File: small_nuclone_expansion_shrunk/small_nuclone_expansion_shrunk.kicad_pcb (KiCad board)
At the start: 2 copper layers, 48.3 x 48.3 mm, 11 parts, among them J1 nuclone_small_left, J2 nuclone_small_right, J3 PINS_1X18, J4 PINS_1X17

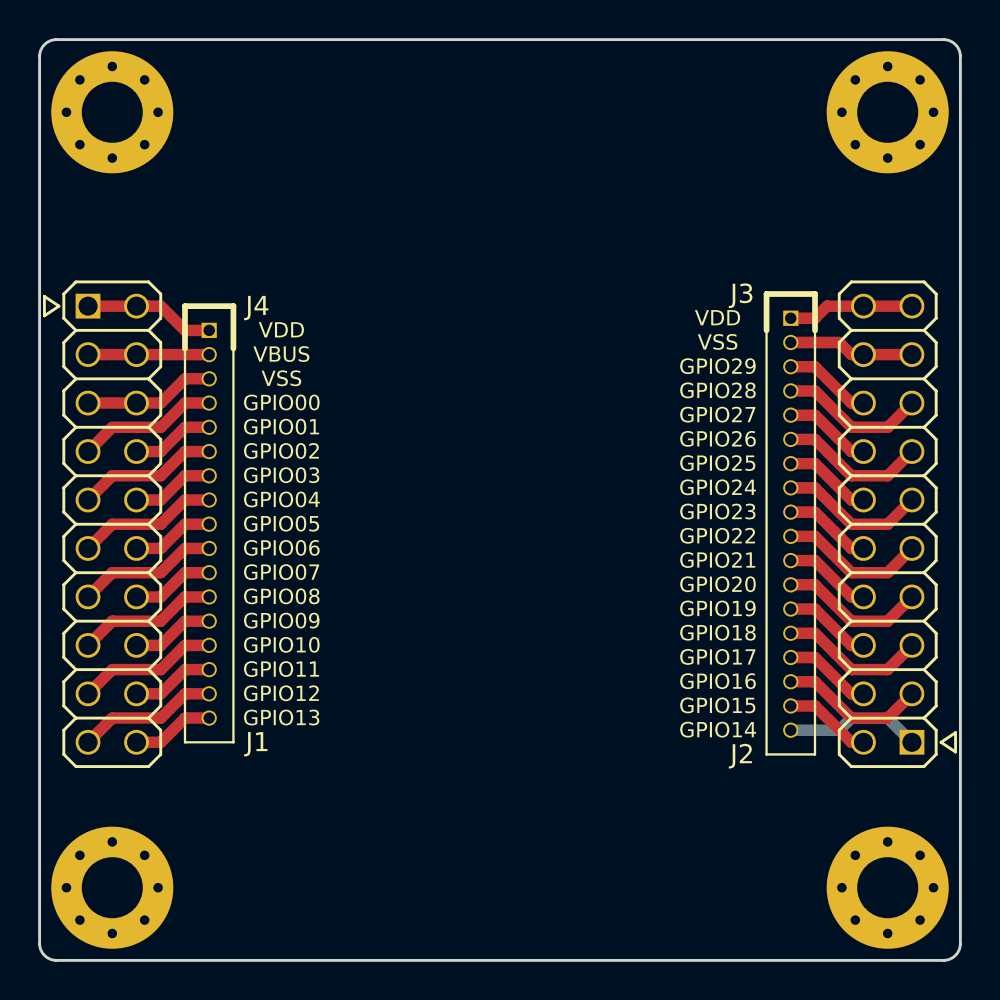
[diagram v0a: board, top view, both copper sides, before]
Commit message: adjusted board outline a bit to make it two square inches
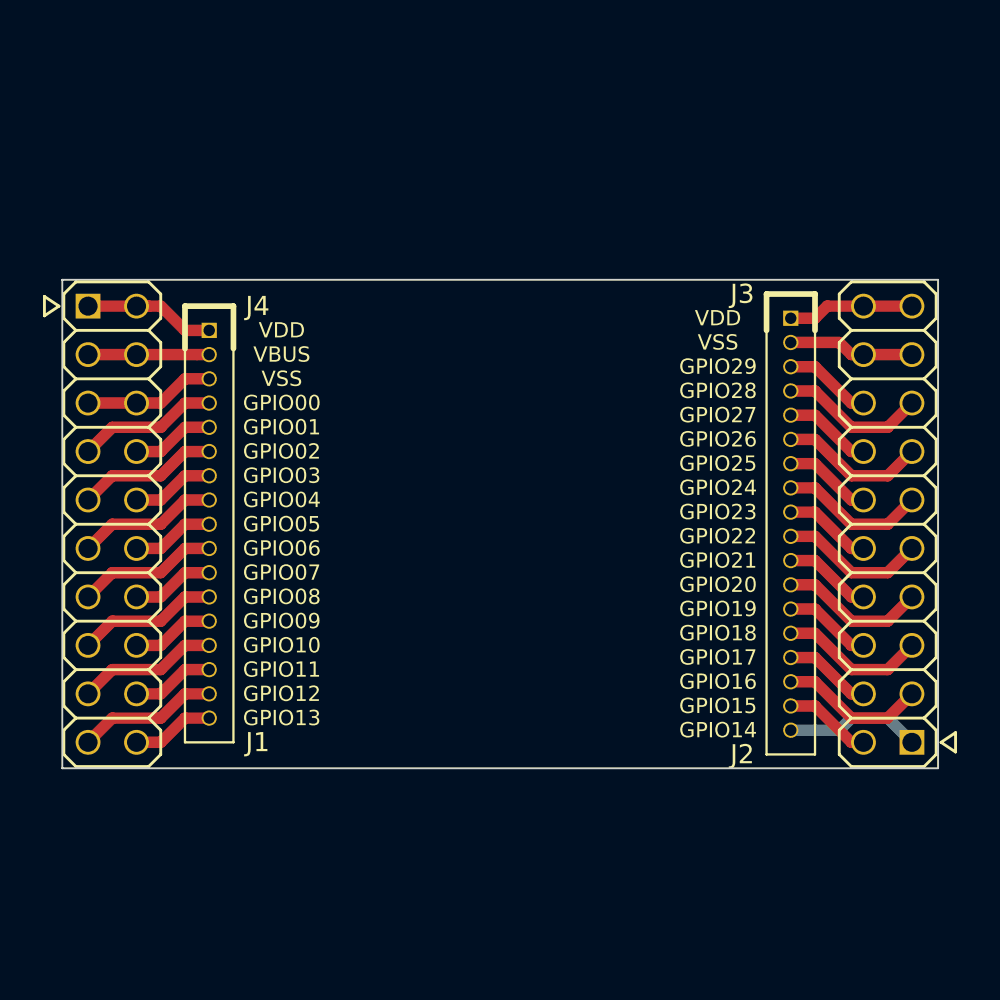
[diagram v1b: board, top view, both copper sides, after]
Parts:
- removed H1, H2, H3, H4: MountingHole, MountingHole:MountingHole_3.2mm_M3_Pad_Via
- moved N1 10.2 mm to (85.2, 91.7)
- moved N2 10.2 mm to (83.7, 95.7)
- moved N3 10.2 mm to (86.0, 97.7)
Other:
- board size 48.3 x 48.3 mm -> 45.9 x 25.6 mm
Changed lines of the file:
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@@
   (general
     (thickness 1.6)
-    (drawings 78)
+    (drawings 74)
     (tracks 127)
     (zones 0)
-    (modules 11)
+    (modules 7)
     (nets 36)
   )
@@
   )
   (module SquantorLabels:Label_Generic (layer B.Cu)
-    (at 83.7 105.9)
+    (at 83.7 95.74)
     (descr "Label for general purpose use")
     (tags Label)
@@
   )
   (module Symbol:OSHW-Symbol_6.7x6mm_SilkScreen (layer B.Cu)
-    (at 85.2 101.9 180)
+    (at 85.2 91.74 180)
     (descr "Open Source Hardware Symbol")
     (tags "Logo Symbol OSHW")
@@
   )
   (module SquantorLabels:Label_Generic (layer B.Cu)
-    (at 86 107.9 180)
+    (at 86 97.74 180)
     (descr "Label for general purpose use")
     (tags Label)
@@
     (fp_line (start -0.5 -0.6) (end 0.5 -0.6) (layer B.SilkS) (width 0.15))
   )
-  (module MountingHole:MountingHole_3.2mm_M3_Pad_Via (layer F.Cu)
-    (at 64.77 64.77)
-    (descr "Mounting Hole 3.2mm, M3")
-    (tags "mounting hole 3.2mm m3")
-    (attr virtual)
-    (fp_text reference H1 (at 0 4.23) (layer F.SilkS) hide
-      (effects (font (size 1 1) (thickness 0.15)))
-    )
-    (fp_text value MountingHole (at 0 4.2) (layer F.Fab) hide
-      (effects (font (size 1 1) (thickness 0.15)))
-    )
-    (fp_circle (center 0 0) (end 3.45 0) (layer F.CrtYd) (width 0.05))
-    (fp_circle (center 0 0) (end 3.2 0) (layer Cmts.User) (width 0.15))
-    (fp_text user %R (at 0.3 0) (layer F.Fab)
-      (effects (font (size 1 1) (thickness 0.15)))
-    )
-    (pad 1 thru_hole circle (at 1.697056 -1.697056) (size 0.8 0.8) (drill 0.5) (layers *.Cu *.Mask))
-    (pad 1 thru_hole circle (at 0 -2.4) (size 0.8 0.8) (drill 0.5) (layers *.Cu *.Mask))
-    (pad 1 thru_hole circle (at -1.697056 -1.697056) (size 0.8 0.8) (drill 0.5) (layers *.Cu *.Mask))
-    (pad 1 thru_hole circle (at -2.4 0) (size 0.8 0.8) (drill 0.5) (layers *.Cu *.Mask))
-    (pad 1 thru_hole circle (at -1.697056 1.697056) (size 0.8 0.8) (drill 0.5) (layers *.Cu *.Mask))
-    (pad 1 thru_hole circle (at 0 2.4) (size 0.8 0.8) (drill 0.5) (layers *.Cu *.Mask))
-    (pad 1 thru_hole circle (at 1.697056 1.697056) (size 0.8 0.8) (drill 0.5) (layers *.Cu *.Mask))
-    (pad 1 thru_hole circle (at 2.4 0) (size 0.8 0.8) (drill 0.5) (layers *.Cu *.Mask))
-    (pad 1 thru_hole circle (at 0 0) (size 6.4 6.4) (drill 3.2) (layers *.Cu *.Mask))
-  )
-  (module MountingHole:MountingHole_3.2mm_M3_Pad_Via (layer F.Cu)
-    (at 64.77 105.41)
-    (descr "Mounting Hole 3.2mm, M3")
-    (tags "mounting hole 3.2mm m3")
-    (attr virtual)
-    (fp_text reference H4 (at 0 -4.2) (layer F.SilkS) hide
-      (effects (font (size 1 1) (thickness 0.15)))
-    )
-    (fp_text value MountingHole (at 0 4.2) (layer F.Fab) hide
-      (effects (font (size 1 1) (thickness 0.15)))
-    )
-    (fp_circle (center 0 0) (end 3.45 0) (layer F.CrtYd) (width 0.05))
-    (fp_circle (center 0 0) (end 3.2 0) (layer Cmts.User) (width 0.15))
-    (fp_text user %R (at 0.3 0) (layer F.Fab)
-      (effects (font (size 1 1) (thickness 0.15)))
-    )
-    (pad 1 thru_hole circle (at 1.697056 -1.697056) (size 0.8 0.8) (drill 0.5) (layers *.Cu *.Mask))
-    (pad 1 thru_hole circle (at 0 -2.4) (size 0.8 0.8) (drill 0.5) (layers *.Cu *.Mask))
-    (pad 1 thru_hole circle (at -1.697056 -1.697056) (size 0.8 0.8) (drill 0.5) (layers *.Cu *.Mask))
-    (pad 1 thru_hole circle (at -2.4 0) (size 0.8 0.8) (drill 0.5) (layers *.Cu *.Mask))
-    (pad 1 thru_hole circle (at -1.697056 1.697056) (size 0.8 0.8) (drill 0.5) (layers *.Cu *.Mask))
-    (pad 1 thru_hole circle (at 0 2.4) (size 0.8 0.8) (drill 0.5) (layers *.Cu *.Mask))
-    (pad 1 thru_hole circle (at 1.697056 1.697056) (size 0.8 0.8) (drill 0.5) (layers *.Cu *.Mask))
-    (pad 1 thru_hole circle (at 2.4 0) (size 0.8 0.8) (drill 0.5) (layers *.Cu *.Mask))
-    (pad 1 thru_hole circle (at 0 0) (size 6.4 6.4) (drill 3.2) (layers *.Cu *.Mask))
-  )
-  (module MountingHole:MountingHole_3.2mm_M3_Pad_Via (layer F.Cu)
-    (at 105.41 105.41)
-    (descr "Mounting Hole 3.2mm, M3")
-    (tags "mounting hole 3.2mm m3")
-    (attr virtual)
-    (fp_text reference H3 (at 0 -4.2) (layer F.SilkS) hide
-      (effects (font (size 1 1) (thickness 0.15)))
-    )
-    (fp_text value MountingHole (at 0 4.2) (layer F.Fab) hide
-      (effects (font (size 1 1) (thickness 0.15)))
-    )
-    (fp_circle (center 0 0) (end 3.45 0) (layer F.CrtYd) (width 0.05))
-    (fp_circle (center 0 0) (end 3.2 0) (layer Cmts.User) (width 0.15))
-    (fp_text user %R (at 0.3 0) (layer F.Fab)
-      (effects (font (size 1 1) (thickness 0.15)))
-    )
-    (pad 1 thru_hole circle (at 1.697056 -1.697056) (size 0.8 0.8) (drill 0.5) (layers *.Cu *.Mask))
-    (pad 1 thru_hole circle (at 0 -2.4) (size 0.8 0.8) (drill 0.5) (layers *.Cu *.Mask))
-    (pad 1 thru_hole circle (at -1.697056 -1.697056) (size 0.8 0.8) (drill 0.5) (layers *.Cu *.Mask))
-    (pad 1 thru_hole circle (at -2.4 0) (size 0.8 0.8) (drill 0.5) (layers *.Cu *.Mask))
-    (pad 1 thru_hole circle (at -1.697056 1.697056) (size 0.8 0.8) (drill 0.5) (layers *.Cu *.Mask))
-    (pad 1 thru_hole circle (at 0 2.4) (size 0.8 0.8) (drill 0.5) (layers *.Cu *.Mask))
-    (pad 1 thru_hole circle (at 1.697056 1.697056) (size 0.8 0.8) (drill 0.5) (layers *.Cu *.Mask))
-    (pad 1 thru_hole circle (at 2.4 0) (size 0.8 0.8) (drill 0.5) (layers *.Cu *.Mask))
-    (pad 1 thru_hole circle (at 0 0) (size 6.4 6.4) (drill 3.2) (layers *.Cu *.Mask))
-  )
-  (module MountingHole:MountingHole_3.2mm_M3_Pad_Via (layer F.Cu)
-    (at 105.41 64.77)
-    (descr "Mounting Hole 3.2mm, M3")
-    (tags "mounting hole 3.2mm m3")
-    (attr virtual)
-    (fp_text reference H2 (at 0 -4.2) (layer F.SilkS) hide
-      (effects (font (size 1 1) (thickness 0.15)))
-    )
-    (fp_text value MountingHole (at 0 4.2) (layer F.Fab) hide
-      (effects (font (size 1 1) (thickness 0.15)))
-    )
-    (fp_circle (center 0 0) (end 3.45 0) (layer F.CrtYd) (width 0.05))
-    (fp_circle (center 0 0) (end 3.2 0) (layer Cmts.User) (width 0.15))
-    (fp_text user %R (at 0.3 0) (layer F.Fab)
-      (effects (font (size 1 1) (thickness 0.15)))
-    )
-    (pad 1 thru_hole circle (at 1.697056 -1.697056) (size 0.8 0.8) (drill 0.5) (layers *.Cu *.Mask))
-    (pad 1 thru_hole circle (at 0 -2.4) (size 0.8 0.8) (drill 0.5) (layers *.Cu *.Mask))
-    (pad 1 thru_hole circle (at -1.697056 -1.697056) (size 0.8 0.8) (drill 0.5) (layers *.Cu *.Mask))
-    (pad 1 thru_hole circle (at -2.4 0) (size 0.8 0.8) (drill 0.5) (layers *.Cu *.Mask))
-    (pad 1 thru_hole circle (at -1.697056 1.697056) (size 0.8 0.8) (drill 0.5) (layers *.Cu *.Mask))
-    (pad 1 thru_hole circle (at 0 2.4) (size 0.8 0.8) (drill 0.5) (layers *.Cu *.Mask))
-    (pad 1 thru_hole circle (at 1.697056 1.697056) (size 0.8 0.8) (drill 0.5) (layers *.Cu *.Mask))
-    (pad 1 thru_hole circle (at 2.4 0) (size 0.8 0.8) (drill 0.5) (layers *.Cu *.Mask))
-    (pad 1 thru_hole circle (at 0 0) (size 6.4 6.4) (drill 3.2) (layers *.Cu *.Mask))
-  )
   (gr_text GPIO14 (at 96.52 97.155) (layer B.SilkS)
     (effects (font (size 0.8 0.8) (thickness 0.12)) (justify mirror))
@@
     (effects (font (size 0.8 0.8) (thickness 0.12)))
   )
-  (gr_arc (start 61.849 108.331) (end 60.96 108.331) (angle -90) (layer Edge.Cuts) (width 0.15))
-  (gr_arc (start 108.331 108.331) (end 108.331 109.22) (angle -90) (layer Edge.Cuts) (width 0.15))
-  (gr_arc (start 108.331 61.849) (end 109.22 61.849) (angle -90) (layer Edge.Cuts) (width 0.15))
-  (gr_arc (start 61.849 61.849) (end 61.849 60.96) (angle -90) (layer Edge.Cuts) (width 0.15))
-  (gr_line (start 108.331 60.96) (end 61.849 60.96) (layer Edge.Cuts) (width 0.15))
-  (gr_line (start 109.22 108.331) (end 109.22 61.849) (layer Edge.Cuts) (width 0.15))
-  (gr_line (start 61.849 109.22) (end 108.331 109.22) (layer Edge.Cuts) (width 0.15))
-  (gr_line (start 60.96 61.849) (end 60.96 108.331) (layer Edge.Cuts) (width 0.15))
+  (gr_line (start 108.05 73.55) (end 62.15 73.55) (layer Edge.Cuts) (width 0.1))
+  (gr_line (start 108.05 99.15) (end 108.05 73.55) (layer Edge.Cuts) (width 0.1))
+  (gr_line (start 62.15 99.15) (end 108.05 99.15) (layer Edge.Cuts) (width 0.1))
+  (gr_line (start 62.15 73.55) (end 62.15 99.15) (layer Edge.Cuts) (width 0.1))
   (segment (start 63.5 77.47) (end 66.04 77.47) (width 0.6) (layer F.Cu) (net 1))
   (segment (start 69.215 77.47) (end 69.85 77.47) (width 0.6) (layer F.Cu) (net 1))
